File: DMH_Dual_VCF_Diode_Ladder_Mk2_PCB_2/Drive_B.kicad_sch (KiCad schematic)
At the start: 25 parts, among them J18 Conn_01x06_PinHeader, Q7 BC548, Q8 BC548, SW8 SW_DPDT_x2, U10 TL074

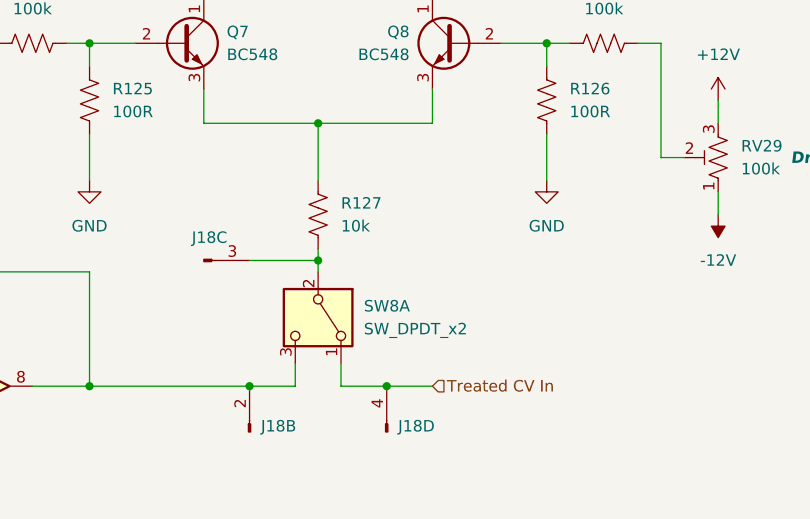
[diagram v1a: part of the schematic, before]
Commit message: Re-exported Gerbers
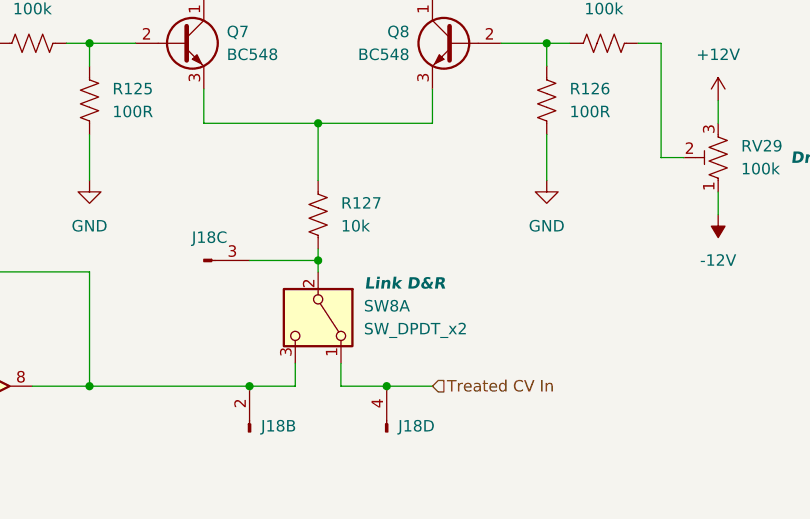
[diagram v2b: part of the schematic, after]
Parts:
- SW8: Function (none) -> Link D&R
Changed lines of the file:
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@@
 		(on_board yes)
 		(dnp no)
-		(fields_autoplaced yes)
 		(property "Reference" "SW8"
 			(at 182.88 118.1099 90)
@@
 			)
 		)
+		(property "Function" "Link D&R"
+			(at 187.452 115.57 90)
+			(effects
+				(font
+					(size 1.27 1.27)
+					(thickness 0.254)
+					(bold yes)
+					(italic yes)
+				)
+			)
+		)
